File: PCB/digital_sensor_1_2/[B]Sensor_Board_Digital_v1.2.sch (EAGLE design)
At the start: 15 parts, among them J1 RJ11REVERSE, J2 RJ45_MX-95001-2881, U2 CC2D23-CHIPCAP2, U3 MS5637-02BA03

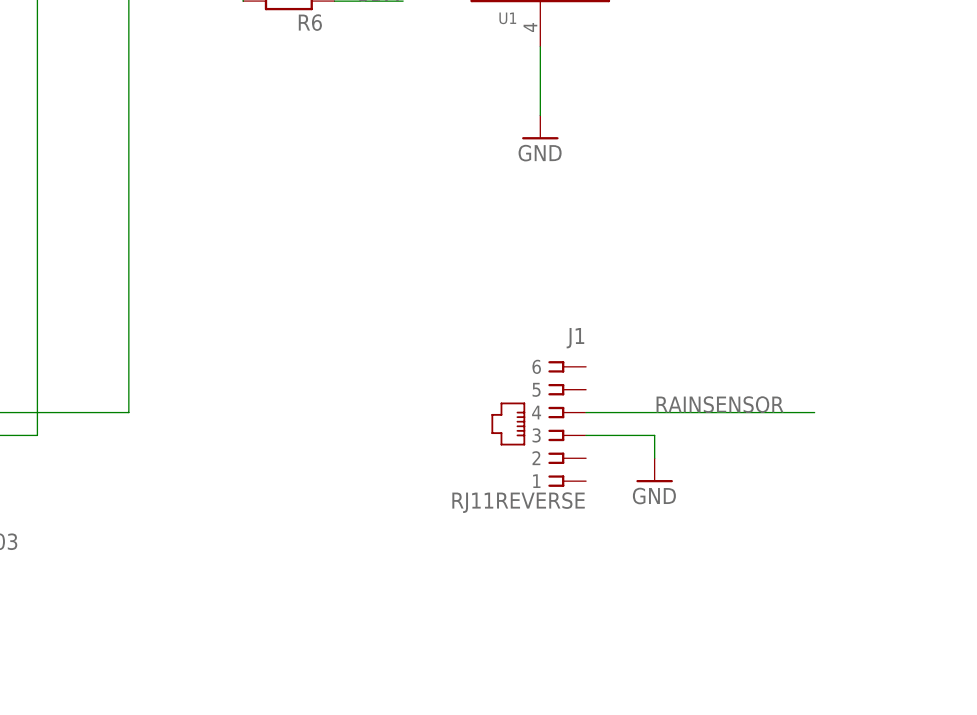
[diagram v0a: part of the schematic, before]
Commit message: Latest revision of PCB with support for RainGauge and some other sensors.
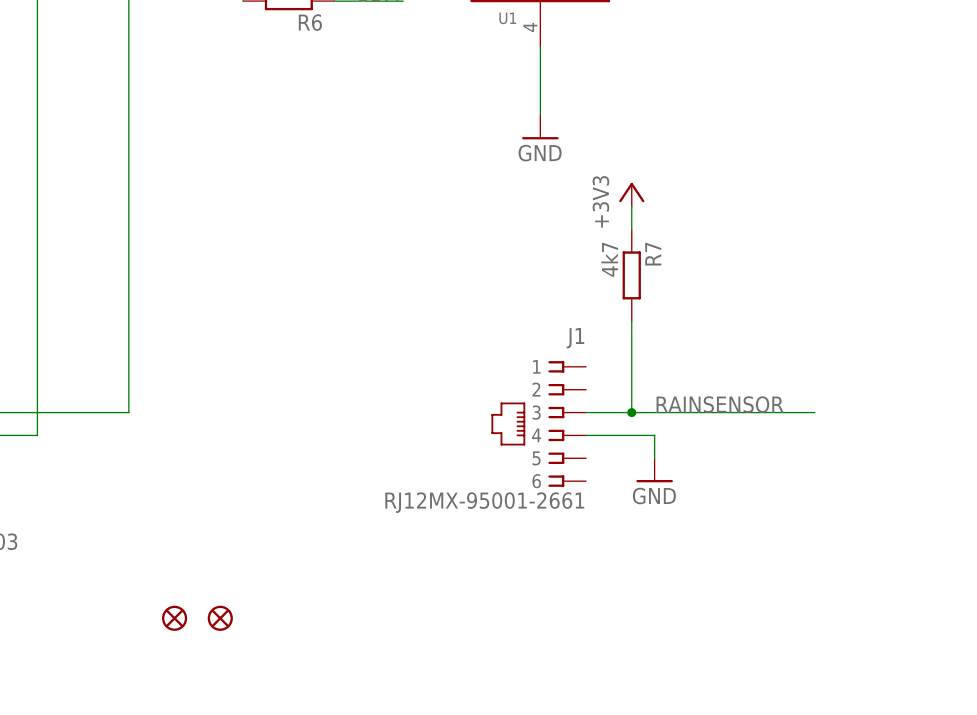
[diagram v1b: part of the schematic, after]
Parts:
- added JP1, JP2: FIDUCIALUFIDUCIAL, SparkFun:FIDUCIALUFIDUCIAL
- added R7: 4k7, rcl:R-EU_R1206
- J1: value RJ11REVERSE -> RJ12MX-95001-2661; device Thomas Egnal Library:RJ11REVERSE -> Thomas Egnal Library:RJ12MX-95001-2661
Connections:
- net +3V3: now also R7.1
- net GND: now also J1.4; no longer J1.3
- net RAINSENSOR: now also J1.3, R7.2; no longer J1.4
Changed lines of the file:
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@@
 <part name="R5" library="rcl" deviceset="R-EU_" device="R1206" value="0R"/>
 <part name="R6" library="rcl" deviceset="R-EU_" device="R1206" value="0R"/>
-<part name="J1" library="Thomas Egnal Library" deviceset="RJ11REVERSE" device=""/>
 <part name="J2" library="Thomas Egnal Library" deviceset="RJ45" device="_MX-95001-2881"/>
 <part name="GND6" library="supply1" deviceset="GND" device=""/>
@@
 <part name="+3V6" library="supply1" deviceset="+3V3" device=""/>
 <part name="GND7" library="supply1" deviceset="GND" device=""/>
+<part name="J1" library="Thomas Egnal Library" deviceset="RJ12" device="MX-95001-2661"/>
+<part name="R7" library="rcl" deviceset="R-EU_" device="R1206" value="4k7"/>
+<part name="+3V7" library="supply1" deviceset="+3V3" device=""/>
+<part name="JP1" library="SparkFun" deviceset="FIDUCIAL" device="UFIDUCIAL"/>
+<part name="JP2" library="SparkFun" deviceset="FIDUCIAL" device="UFIDUCIAL"/>
 </parts>
 <sheets>
@@
 <instance part="R5" gate="G$1" x="48.26" y="139.7"/>
 <instance part="R6" gate="G$1" x="48.26" y="121.92" rot="R180"/>
-<instance part="J1" gate="G$1" x="78.74" y="76.2" rot="MR0"/>
 <instance part="J2" gate="G$1" x="170.18" y="132.08" rot="MR180"/>
 <instance part="GND6" gate="1" x="88.9" y="68.58"/>
@@
 <instance part="+3V6" gate="G$1" x="-2.54" y="99.06"/>
 <instance part="GND7" gate="1" x="-2.54" y="48.26"/>
+<instance part="J1" gate="G$1" x="78.74" y="76.2" rot="MR0"/>
+<instance part="R7" gate="G$1" x="86.36" y="91.44" rot="R270"/>
+<instance part="+3V7" gate="G$1" x="86.36" y="101.6"/>
+<instance part="JP1" gate="G$1" x="35.56" y="53.34"/>
+<instance part="JP2" gate="G$1" x="40.64" y="53.34"/>
 </instances>
 <busses>
@@
 </segment>
 <segment>
-<pinref part="J1" gate="G$1" pin="3"/>
 <pinref part="GND6" gate="1" pin="GND"/>
 <wire x1="81.28" y1="73.66" x2="88.9" y2="73.66" width="0.1524" layer="91"/>
 <wire x1="88.9" y1="73.66" x2="88.9" y2="71.12" width="0.1524" layer="91"/>
+<pinref part="J1" gate="G$1" pin="4"/>
 </segment>
 <segment>
@@
 <wire x1="-22.86" y1="93.98" x2="-22.86" y2="78.74" width="0.1524" layer="91"/>
 <junction x="-2.54" y="93.98"/>
+</segment>
+<segment>
+<pinref part="R7" gate="G$1" pin="1"/>
+<pinref part="+3V7" gate="G$1" pin="+3V3"/>
+<wire x1="86.36" y1="96.52" x2="86.36" y2="99.06" width="0.1524" layer="91"/>
 </segment>
 </net>
@@
 <net name="RAINSENSOR" class="0">
 <segment>
-<pinref part="J1" gate="G$1" pin="4"/>
-<wire x1="81.28" y1="76.2" x2="106.68" y2="76.2" width="0.1524" layer="91"/>
+<wire x1="81.28" y1="76.2" x2="86.36" y2="76.2" width="0.1524" layer="91"/>
 <label x="88.9" y="76.2" size="1.778" layer="95"/>
-</segment>
-<segment>
+<pinref part="J1" gate="G$1" pin="3"/>
+<pinref part="R7" gate="G$1" pin="2"/>
+<wire x1="86.36" y1="76.2" x2="106.68" y2="76.2" width="0.1524" layer="91"/>
+<wire x1="86.36" y1="86.36" x2="86.36" y2="76.2" width="0.1524" layer="91"/>
+<junction x="86.36" y="76.2"/>
+</segment>
+<segment>
